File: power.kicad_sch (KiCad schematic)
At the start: 0 parts

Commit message: Added power domain stuff
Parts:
- added C10, C21, C22, C8: 470pF 50V, Sullivan-Labs:C_0402_1005Metric, symbol Sullivan-Labs:CAP_470pF_50V_0402
- added C11, C12, C13, C14, C9: 22uF 35V, Sullivan-Labs:C_0805_2012Metric, symbol Sullivan-Labs:CAP_22uF_35V_0805
- added C15, C16, C17, C5: 10uF 50V, Sullivan-Labs:C_0805_2012Metric, symbol Sullivan-Labs:CAP_10uF_50V_0805
- added C18, C19, C20, C6, C7: .1uF 50V, Sullivan-Labs:C_0603_1608Metric, symbol Sullivan-Labs:CAP_.1uF_50V_0603
- added C23: .1uF 25V, Sullivan-Labs:C_0402_1005Metric, symbol Sullivan-Labs:CAP_.1uF_25V_0402
- added D2: 30V 800mA, Sullivan-Labs:SC-76, SOD-323, symbol Sullivan-Labs:DIODE 30V 800mA 220mVf
- added D3: 17V TVS, Sullivan-Labs:SOD123W, symbol Sullivan-Labs:DIODE TVS 17Vwm 400W
- added FB1: 440mA 600ohm, Sullivan-Labs:R_0402_1005Metric, symbol Sullivan-Labs:FB_600Ohm_100MHz_0402
- added L1: 1mH, Sullivan-Labs:DR73-102-R, symbol Sullivan-Labs:IND 1mH 260mA
- added Q2: SQJQ131EL, Sullivan-Labs:TO_EL-T1_GE3_VIS, symbol Sullivan-Labs:PMOS SQJQ131EL
- added Q3: 2N7002NXAKR, Sullivan-Labs:SOT95P230X110-3N, symbol Sullivan-Labs:NMOS 190mA 60V
- added R4, R5: 0R, Sullivan-Labs:R_0402_1005Metric, symbol Sullivan-Labs:RES_0R_0402
- added R7, R8: 100k, Sullivan-Labs:R_0402_1005Metric, symbol Sullivan-Labs:RES_100k_0402
- added R9: 510R, Sullivan-Labs:R_0402_1005Metric, symbol Sullivan-Labs:RES_510R_0402
- added U4: 5V 200mA, Sullivan-Labs:SC-74A, SOT-753, symbol Sullivan-Labs:LDO 5Vout 18Vin 200mA
- added U5: 3.3V 200mA, Sullivan-Labs:SC-74A, SOT-753, symbol Sullivan-Labs:LDO 3.3Vout 18Vin 200mA
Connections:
- new net: D2.1, L1.1
- new net: C23.1, Q3.1 (G), R7.1, R9.2
- new net: R5.2, U5.3 (EN)
- new net: C5.1, C6.1, C8.1, FB1.2, R4.1, U4.1 (IN)
- new net: Q2.4, Q3.3 (D), R8.2
- new net: R4.2, U4.3 (EN)
- new net +12V: D2.2, Q2.5
- new net +3.3V: C16.1, C19.1, C22.1, U5.5 (OUT)
- new net +5V: C10.1, C15.1, C18.1, C21.1, C7.1, R5.1, U4.5 (OUT), U5.1 (IN)
- new net GND: C10.2, C11.2, C12.2, C13.2, C14.2, C15.2, C16.2, C17.2, C18.2, C19.2, C20.2, C21.2, C22.2, C23.2, C5.2, C6.2, C7.2, C8.2, C9.2, D3.2 (A), Q3.2 (S), R7.2, U4.2 (GND), U4.4 (NC), U5.2 (GND), U5.4 (NC)
- new net IGN: R9.1
- new net VDC: Q2.1, Q2.2, Q2.3, R8.1
- new net V_FILT: C11.1, C12.1, C13.1, C14.1, C17.1, C20.1, C9.1, D3.1 (K), FB1.1, L1.2

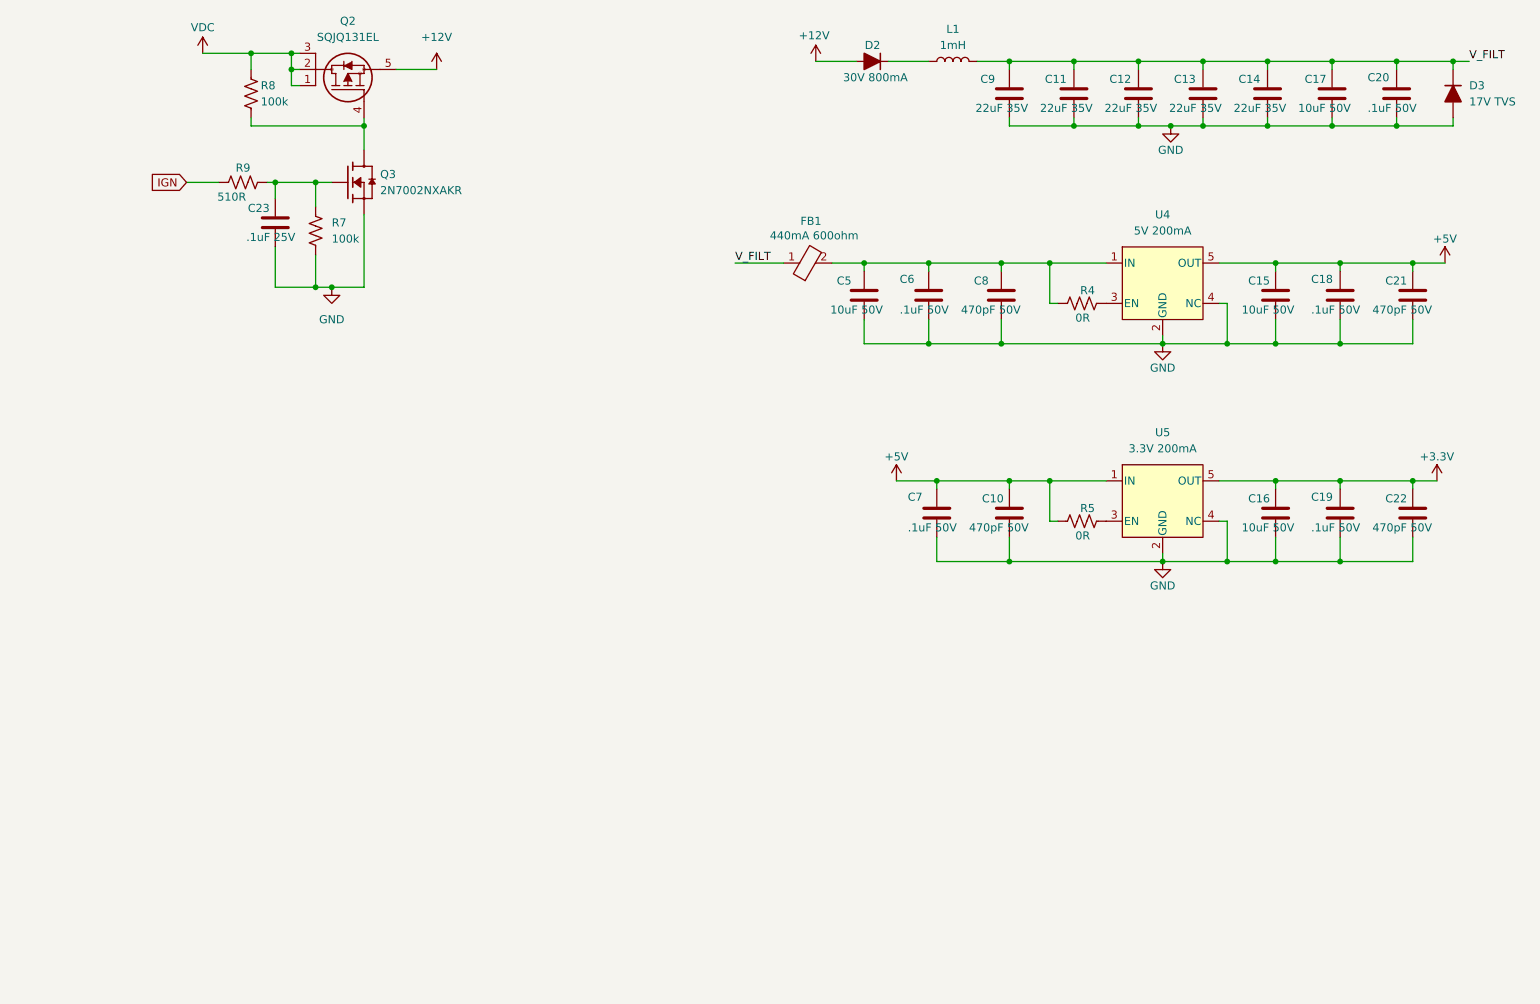
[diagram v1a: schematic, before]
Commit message: Added peripherals page and started gauge control
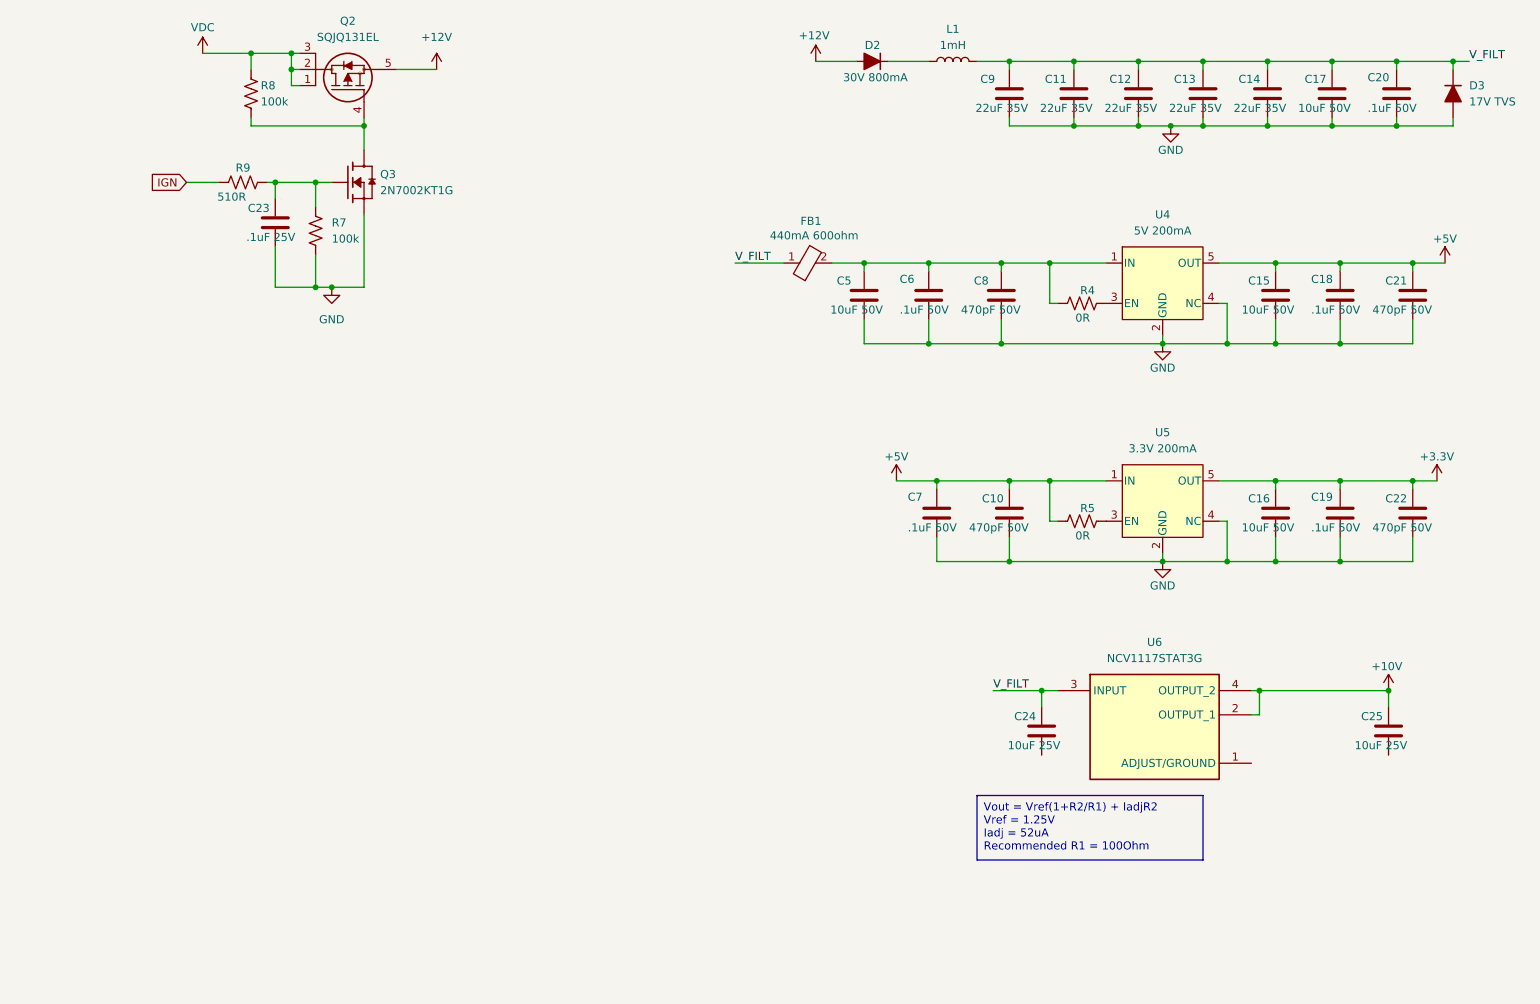
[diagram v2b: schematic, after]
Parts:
- removed Q3: 2N7002NXAKR, Sullivan-Labs:SOT95P230X110-3N, symbol Sullivan-Labs:NMOS 190mA 60V
- added C24, C25: 10uF 25V, Sullivan-Labs:C_0805_2012Metric, symbol Sullivan-Labs:CAP_10uF_25V_0805
- added Q3: 2N7002KT1G, Sullivan-Labs:SOT95P230X110-3N, symbol Sullivan-Labs:NMOS 320mA 60V
- added U6: NCV1117STAT3G, Sullivan-Labs:SOT230P700X180-4N, symbol Sullivan-Labs:LDO Adj 1A 20V
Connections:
- net GND: now also Q3.2 (S)
- net V_FILT: now also C24.1, U6.3 (INPUT)
- net at C23.1, R7.1, R9.2: now also Q3.1 (G)
- net at Q2.4, R8.2: now also Q3.3 (D)
- new net +10V: C25.1, U6.2 (OUTPUT_1), U6.4 (OUTPUT_2)

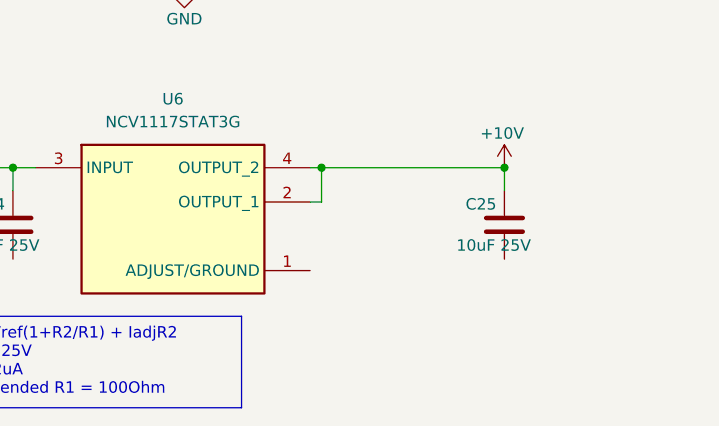
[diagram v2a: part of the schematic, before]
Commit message: Finished gauge power circuit
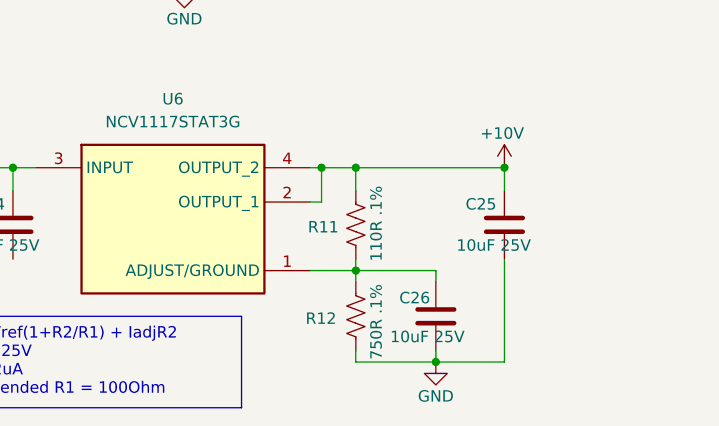
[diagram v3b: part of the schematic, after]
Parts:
- added C26: 10uF 25V, Sullivan-Labs:C_0805_2012Metric, symbol Sullivan-Labs:CAP_10uF_25V_0805
- added R11: 110R .1%, Sullivan-Labs:R_0402_1005Metric, symbol Sullivan-Labs:RES_110R_0402
- added R12: 750R .1%, Sullivan-Labs:R_0402_1005Metric, symbol Sullivan-Labs:RES_750R_0402
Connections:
- net +10V: now also R11.1
- net GND: now also C25.2, C26.2, R12.2
- net at U6.1 (ADJUST/GROUND): now also C26.1, R11.2, R12.1

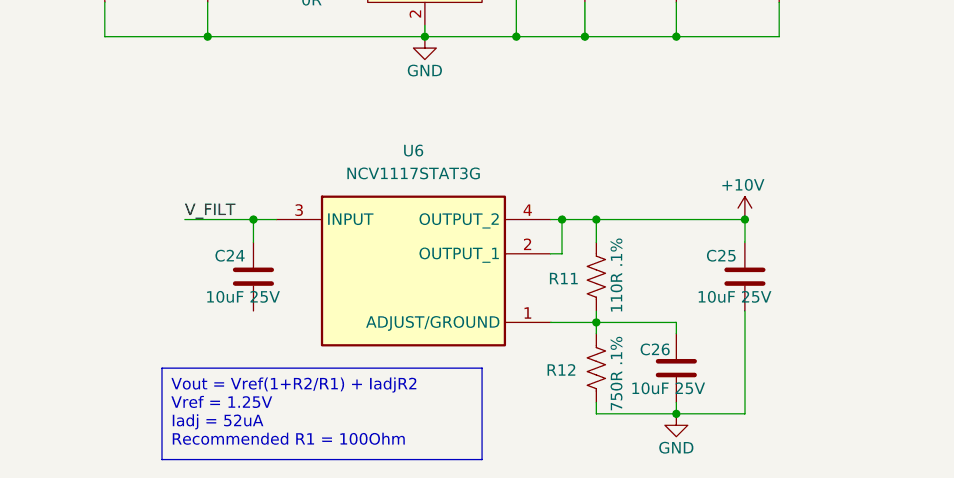
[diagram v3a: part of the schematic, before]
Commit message: Change gauge LDO
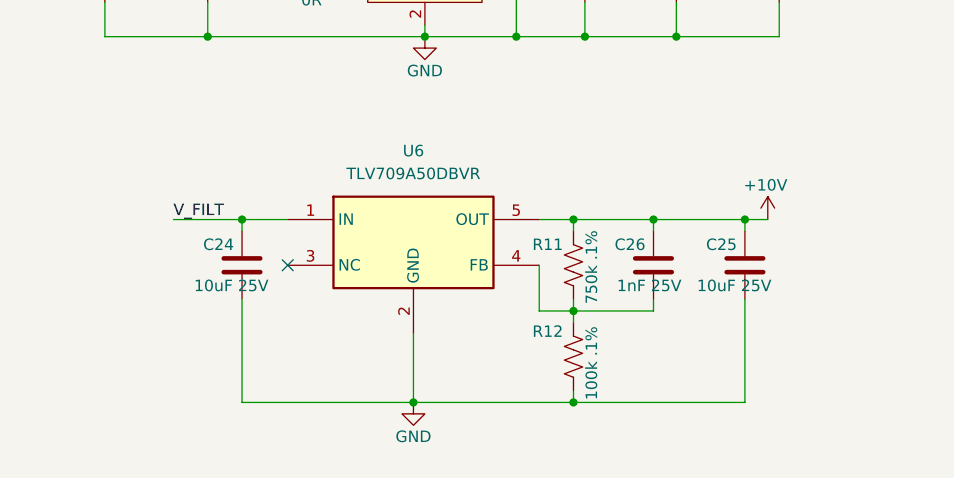
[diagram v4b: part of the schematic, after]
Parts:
- removed C26: 10uF 25V, Sullivan-Labs:C_0805_2012Metric, symbol Sullivan-Labs:CAP_10uF_25V_0805
- removed R11: 110R .1%, Sullivan-Labs:R_0402_1005Metric, symbol Sullivan-Labs:RES_110R_0402
- removed R12: 750R .1%, Sullivan-Labs:R_0402_1005Metric, symbol Sullivan-Labs:RES_750R_0402
- removed U6: NCV1117STAT3G, Sullivan-Labs:SOT230P700X180-4N, symbol Sullivan-Labs:LDO Adj 1A 20V
- added C26: 1nF 25V, Sullivan-Labs:C_0402_1005Metric, symbol Sullivan-Labs:CAP_1nF_25V_0402
- added R11: 750k .1%, Sullivan-Labs:R_0402_1005Metric, symbol Sullivan-Labs:RES_750k_.1%_0402
- added R12: 100k .1%, Sullivan-Labs:R_0402_1005Metric, symbol Sullivan-Labs:RES_100k_.1%_0402
- added U6: TLV709A50DBVR, Sullivan-Labs:SOT95P280X145-5N, symbol Sullivan-Labs:LDO Adj 30V 150mA
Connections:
- net +10V: now also C26.1, R11.1, U6.5 (OUT)
- net GND: now also C24.2, R12.2, U6.2 (GND)
- net V_FILT: now also U6.1 (IN)
- new net: C26.2, R11.2, R12.1, U6.4 (FB)
- no-connect marks 0 -> 1
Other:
- moved on the sheet: C24, C25

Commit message: Added opto-isolated input switches and some sensor stuff
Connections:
- net +10V renamed GAUGEPWR
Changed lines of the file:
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@@
+		)
+	)
+	(global_label "GAUGEPWR"
+		(shape output)
+		(at 245.11 134.62 0)
+		(fields_autoplaced yes)
+		(effects
+			(font
+				(size 1.27 1.27)
+			)
+			(justify left)
+		)
+		(property "Intersheetrefs" "${INTERSHEET_REFS}"
+			(at 258.1947 134.62 0)
+			(effects
+				(font
+					(size 1.27 1.27)
+				)
+				(justify left)
+				(hide yes)
+			)
 		)
 	)
@@
 					(unit 1)
 				)
-			)
-		)
-	)
-	(symbol
-		(lib_id "power:+10V")
-		(at 245.11 134.62 0)
-		(unit 1)
-		(exclude_from_sim no)
-		(in_bom yes)
-		(on_board yes)
-		(dnp no)
-		(property "Reference" "#PWR016"
-			(at 245.11 138.43 0)
-			(effects
-				(font
-					(size 1.27 1.27)
-				)
-				(hide yes)
-			)
-		)
-		(property "Value" "+10V"
-			(at 244.856 130.81 0)
-			(effects
-				(font
-					(size 1.27 1.27)
-				)
-			)
-		)
-		(property "Footprint" ""
-			(at 245.11 134.62 0)
-			(effects
-				(font
-					(size 1.27 1.27)
-				)
-				(hide yes)
-			)
-		)
-		(property "Datasheet" ""
-			(at 245.11 134.62 0)
-			(effects
-				(font
-					(size 1.27 1.27)
-				)
-				(hide yes)
-			)
-		)
-		(property "Description" "Power symbol creates a global label with name \"+10V\""
-			(at 245.11 134.62 0)
-			(effects
-				(font
-					(size 1.27 1.27)
-				)
-				(hide yes)
-			)
-		)
-		(pin "1"
-		)
-		(instances
-			(project ""
-				(path "/d013d610-c58f-4b11-9d18-37fc135ac516/2fe0b40e-9c10-4ff0-b2cd-5720581d147f"
-					(reference "#PWR016")
-					(unit 1)
-				)

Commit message: Small changes to schematic
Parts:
- added C29: 10uF 50V, Sullivan-Labs:C_0805_2012Metric, symbol Sullivan-Labs:CAP_10uF_50V_0805
- added FB2: 440mA 600ohm, Sullivan-Labs:R_0402_1005Metric, symbol Sullivan-Labs:FB_600Ohm_100MHz_0402
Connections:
- net +5V: no longer C10.1, C7.1, R5.1, U5.1 (IN)
- net GND: now also C29.2
- net V_FILT: now also FB2.1
- new net: C10.1, C29.1, C7.1, FB2.2, R5.1, U5.1 (IN)
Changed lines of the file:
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@@
 	(paper "A4")
 	(junction
-		(at 171.45 101.6)
-		(diameter 0)
-		(color 0 0 0 0)
-	)
-	(junction
 		(at 203.2 35.56)
 		(diameter 0)
@@
 	)
 	(junction
+		(at 171.45 114.3)
+		(diameter 0)
+		(color 0 0 0 0)
+	)
+	(junction
 		(at 170.18 80.01)
 		(diameter 0)
@@
 	)
 	(junction
+		(at 171.45 101.6)
+		(diameter 0)
+		(color 0 0 0 0)
+	)
+	(junction
 		(at 223.52 35.56)
 		(diameter 0)
@@
 	)
 	(junction
+		(at 161.29 101.6)
+		(diameter 0)
+		(color 0 0 0 0)
+	)
+	(junction
 		(at 223.52 144.78)
 		(diameter 0)
@@
 	(wire
 		(pts
+			(xy 161.29 101.6) (xy 171.45 101.6)
+		)
+		(stroke
+			(width 0)
+			(type default)
+		)
+	)
+	(wire
+		(pts
 			(xy 224.79 76.2) (xy 224.79 80.01)
 		)
@@
 	(wire
 		(pts
+			(xy 161.29 101.6) (xy 161.29 102.87)
+		)
+		(stroke
+			(width 0)
+			(type default)
+		)
+	)
+	(wire
+		(pts
 			(xy 224.79 67.31) (xy 224.79 68.58)
 		)
@@
 	(wire
 		(pts
+			(xy 161.29 110.49) (xy 161.29 114.3)
+		)
+		(stroke
+			(width 0)
+			(type default)
+		)
+	)
+	(wire
+		(pts
 			(xy 217.17 80.01) (xy 224.79 80.01)
 		)
@@
 	(wire
 		(pts
+			(xy 139.7 101.6) (xy 147.32 101.6)
+		)
+		(stroke
+			(width 0)
+			(type default)
+		)
+	)
+	(wire
+		(pts
 			(xy 189.23 101.6) (xy 189.23 107.95)
 		)
@@
 	(wire
 		(pts
+			(xy 154.94 101.6) (xy 161.29 101.6)
+		)
+		(stroke
+			(width 0)
+			(type default)
+		)
+	)
+	(wire
+		(pts
 			(xy 234.95 67.31) (xy 234.95 68.58)
 		)
@@
 	(wire
 		(pts
-			(xy 165.1 101.6) (xy 171.45 101.6)
-		)
-		(stroke
-			(width 0)
-			(type default)
-		)
-	)
-	(wire
-		(pts
 			(xy 181.61 80.01) (xy 207.01 80.01)
 		)
@@
 	(wire
 		(pts
+			(xy 161.29 114.3) (xy 171.45 114.3)
+		)
+		(stroke
+			(width 0)
+			(type default)
+		)
+	)
+	(wire
+		(pts
 			(xy 182.88 44.45) (xy 182.88 45.72)
 		)
@@
 		)
 	)
+	(text_box "Make supplies independent of each other in case of bad external wiring"
+		(exclude_from_sim no)
+		(at 125.73 77.47 0)
+		(size 26.67 13.97)
+		(stroke
+			(width 0)
+			(type default)
+		)
+		(fill
+			(type color)
+			(color 255 255 194 1)
+		)
+		(effects
+			(font
+				(size 1.27 1.27)
+			)
+			(justify left top)
+		)
+	)
+	(label "V_FILT"
+		(at 139.7 101.6 0)
+		(fields_autoplaced yes)
+		(effects
+			(font
+				(size 1.27 1.27)
+			)
+			(justify left bottom)
+		)
+	)
 	(label "V_FILT"
 		(at 139.7 67.31 0)
@@
 	)
 	(symbol
-		(lib_id "power:+5V")
-		(at 165.1 101.6 0)
-		(unit 1)
-		(exclude_from_sim no)
-		(in_bom yes)
-		(on_board yes)
-		(dnp no)
-		(property "Reference" "#PWR06"
-			(at 165.1 105.41 0)
-			(effects
-				(font
-					(size 1.27 1.27)
-				)
-				(hide yes)
-			)
-		)
-		(property "Value" "+5V"
-			(at 165.1 97.79 0)
-			(effects
-				(font
-					(size 1.27 1.27)
-				)
-			)
-		)
-		(property "Footprint" ""
-			(at 165.1 101.6 0)
-			(effects
-				(font
-					(size 1.27 1.27)
-				)
-				(hide yes)
-			)
-		)
-		(property "Datasheet" ""
-			(at 165.1 101.6 0)
-			(effects
-				(font
-					(size 1.27 1.27)
-				)
-				(hide yes)
-			)
-		)
-		(property "Description" "Power symbol creates a global label with name \"+5V\""
-			(at 165.1 101.6 0)
-			(effects
-				(font
-					(size 1.27 1.27)
-				)
-				(hide yes)
-			)
-		)
-		(pin "1"
-		)
-		(instances
-			(project "cooler-master"
-				(path "/d013d610-c58f-4b11-9d18-37fc135ac516/2fe0b40e-9c10-4ff0-b2cd-5720581d147f"
-					(reference "#PWR06")
-					(unit 1)
-				)
-			)
-		)
-	)
-	(symbol
 		(lib_id "Sullivan-Labs:CAP_.1uF_50V_0603")
 		(at 234.95 72.39 0)
@@
 	)
 	(symbol
+		(lib_id "Sullivan-Labs:CAP_10uF_50V_0805")
+		(at 161.29 106.68 0)
+		(unit 1)
+		(exclude_from_sim no)
+		(in_bom yes)
+		(on_board yes)
+		(dnp no)
+		(property "Reference" "C29"
+			(at 156.972 104.394 0)
+			(effects
+				(font
+					(size 1.27 1.27)
+				)
+				(justify left)
+			)
+		)
+		(property "Value" "10uF 50V"
+			(at 155.956 108.966 0)
+			(effects
+				(font
+					(size 1.27 1.27)
+				)
+				(justify left)
+			)
+		)
+		(property "Footprint" "Sullivan-Labs:C_0805_2012Metric"
+			(at 162.2552 110.49 0)
+			(effects
+				(font
+					(size 1.27 1.27)
+				)
+				(hide yes)
+			)
+		)
+		(property "Datasheet" "~"
+			(at 161.29 106.68 0)
+			(effects
+				(font
+					(size 1.27 1.27)
+				)
+				(hide yes)
+			)
+		)
+		(property "Description" "10uF 50V 0805 Capacitor"
+			(at 161.29 106.68 0)
+			(effects
+				(font
+					(size 1.27 1.27)
+				)
+				(hide yes)
+			)
+		)
+		(property "Manufacturer" "Murata Electronics"
+			(at 161.29 106.68 0)
+			(effects
+				(font
+					(size 1.27 1.27)
+				)
+				(hide yes)
+			)
+		)
+		(property "PN" "GRM21BR61H106ME43L"
+			(at 161.29 106.68 0)
+			(effects
+				(font
+					(size 1.27 1.27)
+				)
+				(hide yes)
+			)
+		)
+		(pin "1"
+		)
+		(pin "2"
+		)
+		(instances
+			(project "cooler-master"
+				(path "/d013d610-c58f-4b11-9d18-37fc135ac516/2fe0b40e-9c10-4ff0-b2cd-5720581d147f"
+					(reference "C29")
+					(unit 1)
+				)
+			)
+		)
+	)
+	(symbol
 		(lib_id "power:GND")
 		(at 76.2 71.12 0)
@@
 					(unit 1)
 				)
+			)
+		)
+	)
+	(symbol
+		(lib_id "Sullivan-Labs:FB_600Ohm_100MHz_0402")
+		(at 147.32 101.6 0)
+		(unit 1)
+		(exclude_from_sim no)
+		(in_bom yes)
+		(on_board yes)
+		(dnp no)
+		(property "Reference" "FB2"
+			(at 151.638 94.996 0)
+			(effects
+				(font
+					(size 1.27 1.27)
+				)
+			)
+		)
+		(property "Value" "440mA 600ohm"
+			(at 152.146 97.282 0)
+			(effects
+				(font
+					(size 1.27 1.27)
+				)
+			)
+		)
+		(property "Footprint" "Sullivan-Labs:R_0402_1005Metric"
+			(at 163.83 196.52 0)
+			(effects
+				(font
+					(size 1.27 1.27)
+				)
+				(justify left top)
+				(hide yes)
+			)
+		)
+		(property "Datasheet" "https://product.tdk.com/system/files/dam/doc/product/emc/emc/beads/catalog/beads_commercial_signal_mmz1005-h_en.pdf"
+			(at 163.83 296.52 0)
+			(effects
+				(font
+					(size 1.27 1.27)
+				)
+				(justify left top)
+				(hide yes)
+			)
+		)
+		(property "Description" "Chip Beads, |Z|=600? at 100MHz, L x W x T :"
+			(at 147.32 101.6 0)
+			(effects
+				(font
+					(size 1.27 1.27)
+				)
+				(hide yes)
+			)
+		)
+		(property "Manufacturer" "TDK-Lambda"
+			(at 163.83 796.52 0)
+			(effects
+				(font
+					(size 1.27 1.27)
+				)
+				(justify left top)
+				(hide yes)
+			)
+		)
+		(property "PN" "MMZ1005S601HT000"
+			(at 163.83 896.52 0)
+			(effects
+				(font
+					(size 1.27 1.27)
+				)
+				(justify left top)
+				(hide yes)
+			)
+		)
+		(pin "2"
+		)
+		(pin "1"
+		)
+		(instances
+			(project "cooler-master"
+				(path "/d013d610-c58f-4b11-9d18-37fc135ac516/2fe0b40e-9c10-4ff0-b2cd-5720581d147f"
+					(reference "FB2")
+					(unit 1)
+				)
